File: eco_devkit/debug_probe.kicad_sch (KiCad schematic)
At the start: 30 parts, among them J10 SWD Interface, J9 USB_C_Receptacle_USB2.0_16P, Y2 ABM8-272-T3

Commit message: Corrige footprints.
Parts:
- D8: footprint Diode_THT:D_DO-41_SOD81_P10.16mm_Horizontal -> Diode_SMD:D_SOD-123F
- renumbered J9 to J8, J10 to J9
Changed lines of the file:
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@@
 		(on_board yes)
 		(dnp no)
-		(property "Reference" "J10"
+		(property "Reference" "J9"
 			(at 89.662 183.896 0)
 			(effects
@@
 			(project ""
 				(path "/308cd3d6-c3d9-49fe-9127-06fda61df52b/c6fed0ca-04fe-4a1a-8542-8833eebee5d1"
-					(reference "J10")
+					(reference "J9")
 					(unit 1)
 				)
@@
 			)
 		)
-		(property "Footprint" "Diode_THT:D_DO-41_SOD81_P10.16mm_Horizontal"
+		(property "Footprint" "Diode_SMD:D_SOD-123F"
 			(at 63.5 45.085 0)
 			(effects
@@
 		(dnp no)
 		(fields_autoplaced yes)
-		(property "Reference" "J9"
+		(property "Reference" "J8"
 			(at 38.1 41.91 0)
 			(effects
@@
 			(project "eco_devkit"
 				(path "/308cd3d6-c3d9-49fe-9127-06fda61df52b/c6fed0ca-04fe-4a1a-8542-8833eebee5d1"
-					(reference "J9")
+					(reference "J8")
 					(unit 1)
 				)

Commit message: footprint completed
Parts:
- removed C30: 10u, Capacitor_SMD:C_0402_1005Metric, symbol Device:C_Small
- removed NCP2: NCP1117ST50T3G, lib:NCP1117ST50T3G, symbol rp2350b-qfn80:NCP1117
- R39: renamed from R42; footprint Footprint Resistor_SMD:R_0402_1005Metric 0 0 Centro Centro 0 0 -> Resistor_SMD:R_0402_1005Metric
- R40: renamed from R43; MPN RC0402JR-0727RL -> RCS040227R0FKED
- R41: renamed from R44; MPN RC0402JR-0727RL -> RCS040227R0FKED
- U1: renamed from U2; value ~ -> RP2040
- Y2: footprint ABM8_272_T3:XTAL_ABM8-272-T3 -> lib:ABM8-272-T3
- renumbered C31 to C30, C32 to C31, C33 to C32, C34 to C33, C35 to C34, C36 to C35, C37 to C36, C38 to C37, C39 to C38, C40 to C39, C41 to C40, R38 to R35, R39 to R36, R40 to R37, R41 to R38
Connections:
- net VBUS renamed +VBUS
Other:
- moved on the sheet: D8, J8, R36, R37

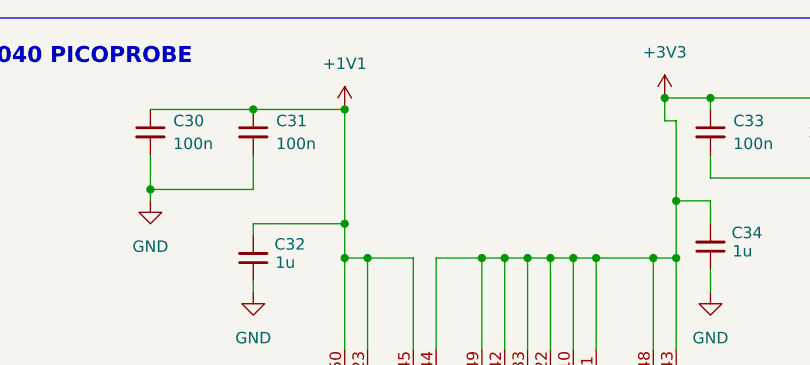
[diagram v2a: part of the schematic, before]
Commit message: Add all nets
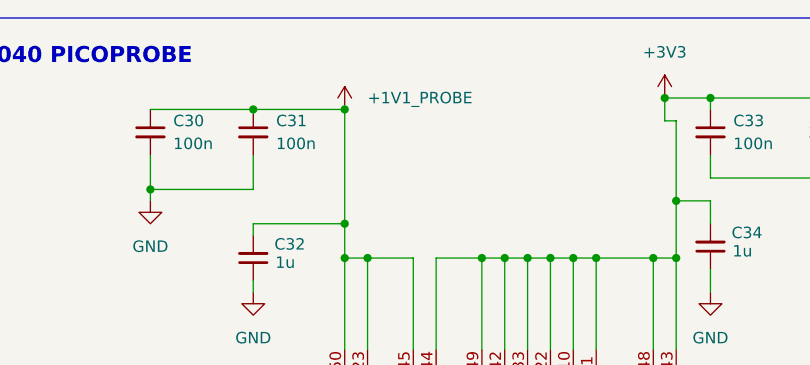
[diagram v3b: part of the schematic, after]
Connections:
- net +1V1 renamed +1V1_PROBE
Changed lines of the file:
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@@
 			)
 		)
-		(property "Value" "+1V1"
-			(at 173.99 19.05 0)
+		(property "Value" "+1V1_PROBE"
+			(at 176.53 22.8599 0)
 			(effects
 				(font
 					(size 1.27 1.27)
 				)
+				(justify left)
 			)
 		)
